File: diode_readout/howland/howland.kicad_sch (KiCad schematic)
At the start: 8 parts, among them J1 Conn_01x04, J2 JST_SH_Conn_01x04_i2c_horizon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

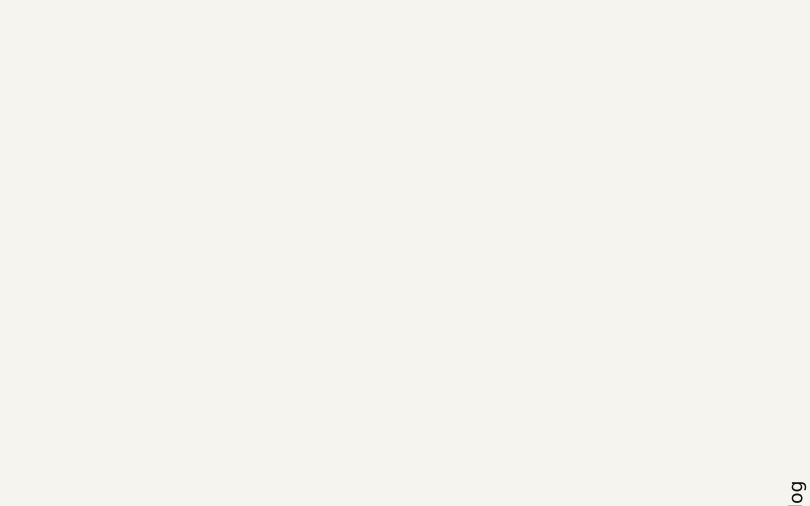
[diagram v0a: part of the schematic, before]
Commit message: add sq_lockin_v8 and tweaks to howland diode_readout
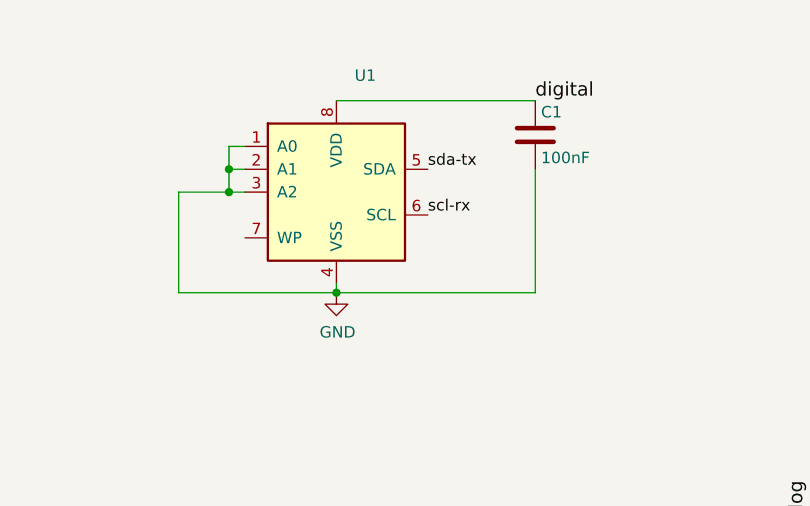
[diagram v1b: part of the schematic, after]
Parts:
- added C1: 100nF, Capacitor_SMD:C_0402_1005Metric, symbol Device:C
- added U1: (no value), symbol Memory_NVRAM:FM24C64C
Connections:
- net GND: now also U1.1 (A0), U1.2 (A1), U1.3 (A2), U1.4 (VSS)
- net VD: now also C1.1, U1.8 (VDD)
- net scl-rx: now also U1.6 (SCL)
- net sda-tx: now also U1.5 (SDA)

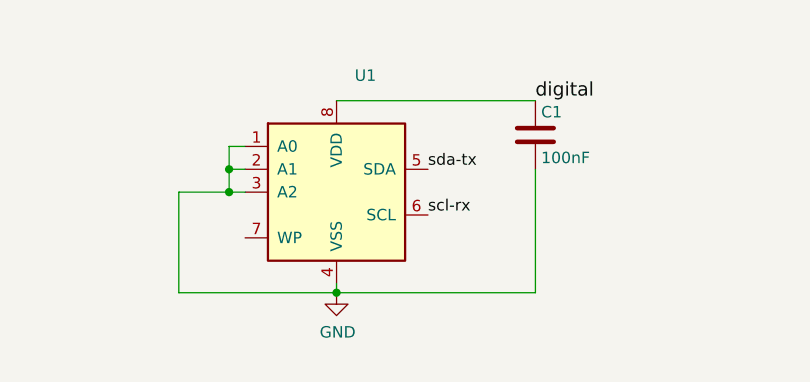
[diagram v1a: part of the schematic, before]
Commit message: Commit changes to howland current source diode readout: 1.  Add 1Mohm shorts bettern V+ and I+  as well as V- and I- to mimic      this will mimic the two wire readout behaviour when the diode gets      disconnected. 2.  Add FRAM chip, 512kbits or 64kBytes of memory
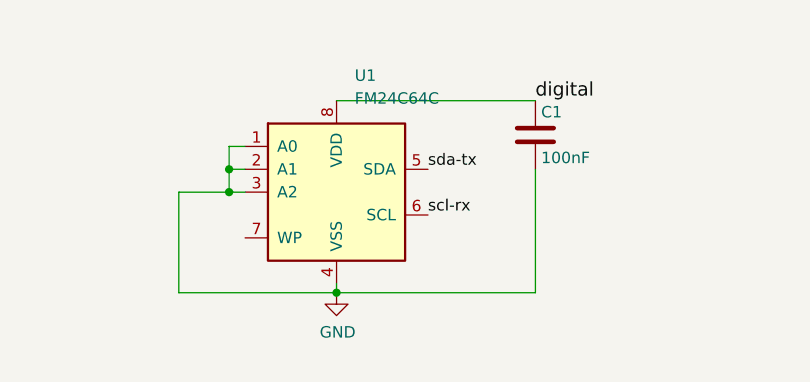
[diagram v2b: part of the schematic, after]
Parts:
- U1: value (none) -> FM24C64C; footprint (none) -> Package_SO:SOIC-8_3.9x4.9mm_P1.27mm
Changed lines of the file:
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@@
       (effects (font (size 1.27 1.27)) (justify left))
     )
-    (property "Value" "" (id 1) (at 110.9854 35.56 0)
+    (property "Value" "FM24C64C" (id 1) (at 110.9854 35.56 0)
       (effects (font (size 1.27 1.27)) (justify left))
     )
-    (property "Footprint" "" (id 2) (at 108.966 45.974 0)
+    (property "Footprint" "Package_SO:SOIC-8_3.9x4.9mm_P1.27mm" (id 2) (at 108.966 45.974 0)
       (effects (font (size 1.27 1.27)) hide)
     )
@@
       (reference "R2") (unit 1) (value "10K") (footprint "Resistor_SMD:R_0603_1608Metric_Pad1.05x0.95mm_HandSolder")
     )
+    (path "/00000000-0000-0000-0000-000059ed3d7b/cb59bfe4-78b3-4525-a18e-6016f07a38e4"
+      (reference "R3") (unit 1) (value "1M") (footprint "Resistor_SMD:R_0402_1005Metric")
+    )
+    (path "/00000000-0000-0000-0000-000059ed3d7b/393f0e56-c2d5-4ea4-8463-50265bc94d2d"
+      (reference "R4") (unit 1) (value "1M") (footprint "Resistor_SMD:R_0402_1005Metric")
+    )
     (path "/00000000-0000-0000-0000-000059ed3d7b/00000000-0000-0000-0000-000059ed1265"
-      (reference "R3") (unit 1) (value "100K") (footprint "Resistor_SMD:R_0402_1005Metric")
+      (reference "R5") (unit 1) (value "100K") (footprint "Resistor_SMD:R_0402_1005Metric")
     )
     (path "/00000000-0000-0000-0000-000059ed3d7b/00000000-0000-0000-0000-000059ed126c"
-      (reference "R4") (unit 1) (value "100K") (footprint "Resistor_SMD:R_0402_1005Metric")
+      (reference "R6") (unit 1) (value "100K") (footprint "Resistor_SMD:R_0402_1005Metric")
     )
     (path "/00000000-0000-0000-0000-000059ed3d7b/0a00994f-3fc0-414a-8e46-3a4bdcea5eb2/5aa91f3c-0195-4e75-88c2-51064725621d"
-      (reference "R5") (unit 1) (value "10K") (footprint "Resistor_SMD:R_0805_2012Metric")
+      (reference "R7") (unit 1) (value "10K") (footprint "Resistor_SMD:R_0805_2012Metric")
     )
     (path "/00000000-0000-0000-0000-000059ed3d7b/0a00994f-3fc0-414a-8e46-3a4bdcea5eb2/cc9e71ff-e12c-4106-95ad-954289c2f7e3"
-      (reference "R6") (unit 1) (value "10K") (footprint "Resistor_SMD:R_0805_2012Metric")
+      (reference "R8") (unit 1) (value "10K") (footprint "Resistor_SMD:R_0805_2012Metric")
     )
     (path "/00000000-0000-0000-0000-000059ed3d7b/0a00994f-3fc0-414a-8e46-3a4bdcea5eb2/a90a73b8-661a-4ba5-948b-2c2ada5eb5a5"
-      (reference "R7") (unit 1) (value "125K") (footprint "Resistor_SMD:R_0805_2012Metric")
+      (reference "R9") (unit 1) (value "125K") (footprint "Resistor_SMD:R_0805_2012Metric")
     )
     (path "/00000000-0000-0000-0000-000059ed3d7b/0a00994f-3fc0-414a-8e46-3a4bdcea5eb2/3430e4dd-38e6-4a37-ae77-90080133b97b"
-      (reference "R8") (unit 1) (value "12.7M") (footprint "Resistor_SMD:R_0805_2012Metric")
+      (reference "R10") (unit 1) (value "12.7M") (footprint "Resistor_SMD:R_0805_2012Metric")
     )
     (path "/00000000-0000-0000-0000-000059ed3d7b/0a00994f-3fc0-414a-8e46-3a4bdcea5eb2/5d00d18b-d30c-4aba-8513-d532618dc371"
-      (reference "R9") (unit 1) (value "10K") (footprint "Resistor_SMD:R_0805_2012Metric")
+      (reference "R11") (unit 1) (value "10K") (footprint "Resistor_SMD:R_0805_2012Metric")
     )
     (path "/00000000-0000-0000-0000-000059ed3d7b/0a00994f-3fc0-414a-8e46-3a4bdcea5eb2/63c4fe4d-2f4e-4b3c-a990-4f916aa9930d"
-      (reference "R10") (unit 1) (value "0") (footprint "Resistor_SMD:R_0603_1608Metric_Pad0.98x0.95mm_HandSolder")
+      (reference "R12") (unit 1) (value "0") (footprint "Resistor_SMD:R_0603_1608Metric_Pad0.98x0.95mm_HandSolder")
     )
     (path "/00000000-0000-0000-0000-000059ed3d7b/0a00994f-3fc0-414a-8e46-3a4bdcea5eb2/4c7508f6-a275-40c9-9d80-35a0598d72c4"
@@
       (reference "U3") (unit 3) (value "TLV2782IDGKR") (footprint "Package_SO:VSSOP-8_3.0x3.0mm_P0.65mm")
     )
-    (path "/00000000-0000-0000-0000-000059ed3d7b/0a00994f-3fc0-414a-8e46-3a4bdcea5eb2/5cbea609-3336-48c5-807b-8f275a8e6dc1"
-      (reference "U4") (unit 1) (value "REF3225AMDBVREP") (footprint "Package_TO_SOT_SMD:SOT-23-6")
+    (path "/00000000-0000-0000-0000-000059ed3d7b/0a00994f-3fc0-414a-8e46-3a4bdcea5eb2/3ccb3e27-d022-4f68-b9b2-be66e341ab1b"
+      (reference "U4") (unit 1) (value "ADR391") (footprint "Package_TO_SOT_SMD:TSOT-23-5_HandSoldering")
     )
     (path "/00000000-0000-0000-0000-000059ed3d7b/0a00994f-3fc0-414a-8e46-3a4bdcea5eb2/d62bbf6c-bcf2-4b7a-9470-80c869ae73db"

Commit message: Keep boards up to date
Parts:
- U1: value FM24C64C -> (none); footprint Package_SO:SOIC-8_3.9x4.9mm_P1.27mm -> (none)
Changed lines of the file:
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@@
       (effects (font (size 1.27 1.27)) (justify left))
     )
-    (property "Value" "FM24C64C" (id 1) (at 110.9854 35.56 0)
+    (property "Value" "" (id 1) (at 110.9854 35.56 0)
       (effects (font (size 1.27 1.27)) (justify left))
     )
-    (property "Footprint" "Package_SO:SOIC-8_3.9x4.9mm_P1.27mm" (id 2) (at 108.966 45.974 0)
-      (effects (font (size 1.27 1.27)) hide)
-    )
-    (property "Datasheet" "http://www.cypress.com/file/41651/download" (id 3) (at 103.886 37.084 0)
+    (property "Footprint" "" (id 2) (at 108.966 45.974 0)
+      (effects (font (size 1.27 1.27)) hide)
+    )
+    (property "Datasheet" "https://datasheet.lcsc.com/lcsc/1806121739_Cypress-Semicon-FM24V05-GTR_C66021.pdf" (id 3) (at 103.886 37.084 0)
       (effects (font (size 1.27 1.27)) hide)
     )
@@
     )
     (path "/ab88f3e0-e707-48e0-91f8-7ac28f1ec265"
-      (reference "U1") (unit 1) (value "FM24C64C") (footprint "Package_SO:SOIC-8_3.9x4.9mm_P1.27mm")
+      (reference "U1") (unit 1) (value "FM24V05") (footprint "Package_SO:SOIC-8_3.9x4.9mm_P1.27mm")
     )
     (path "/00000000-0000-0000-0000-000059ed3d7b/e9890516-b047-4c9e-9731-dd57dc45efd4"

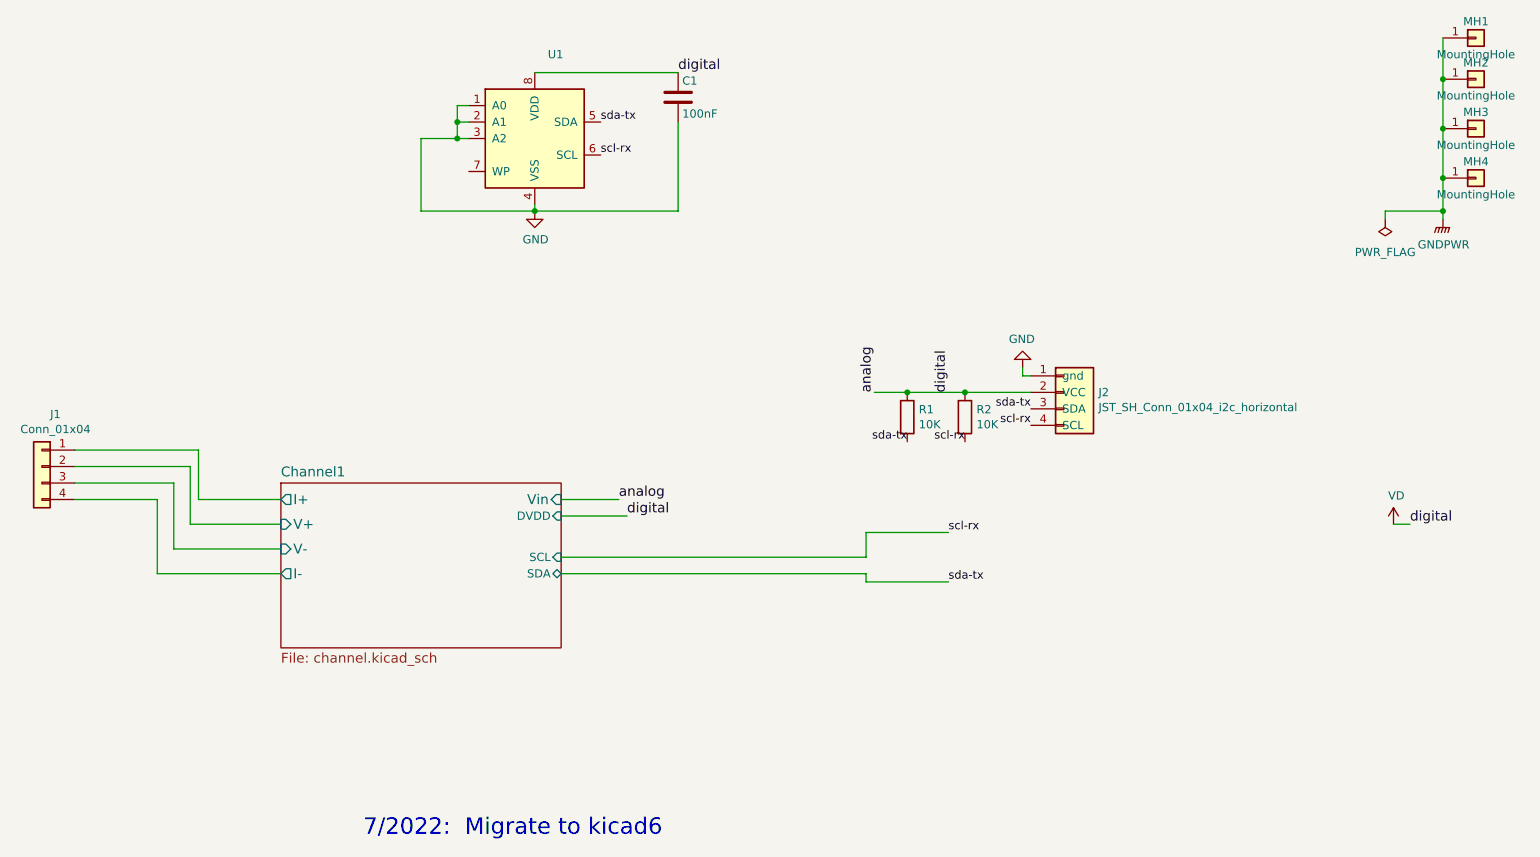
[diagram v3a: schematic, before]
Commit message: Add tweaks to diode readout
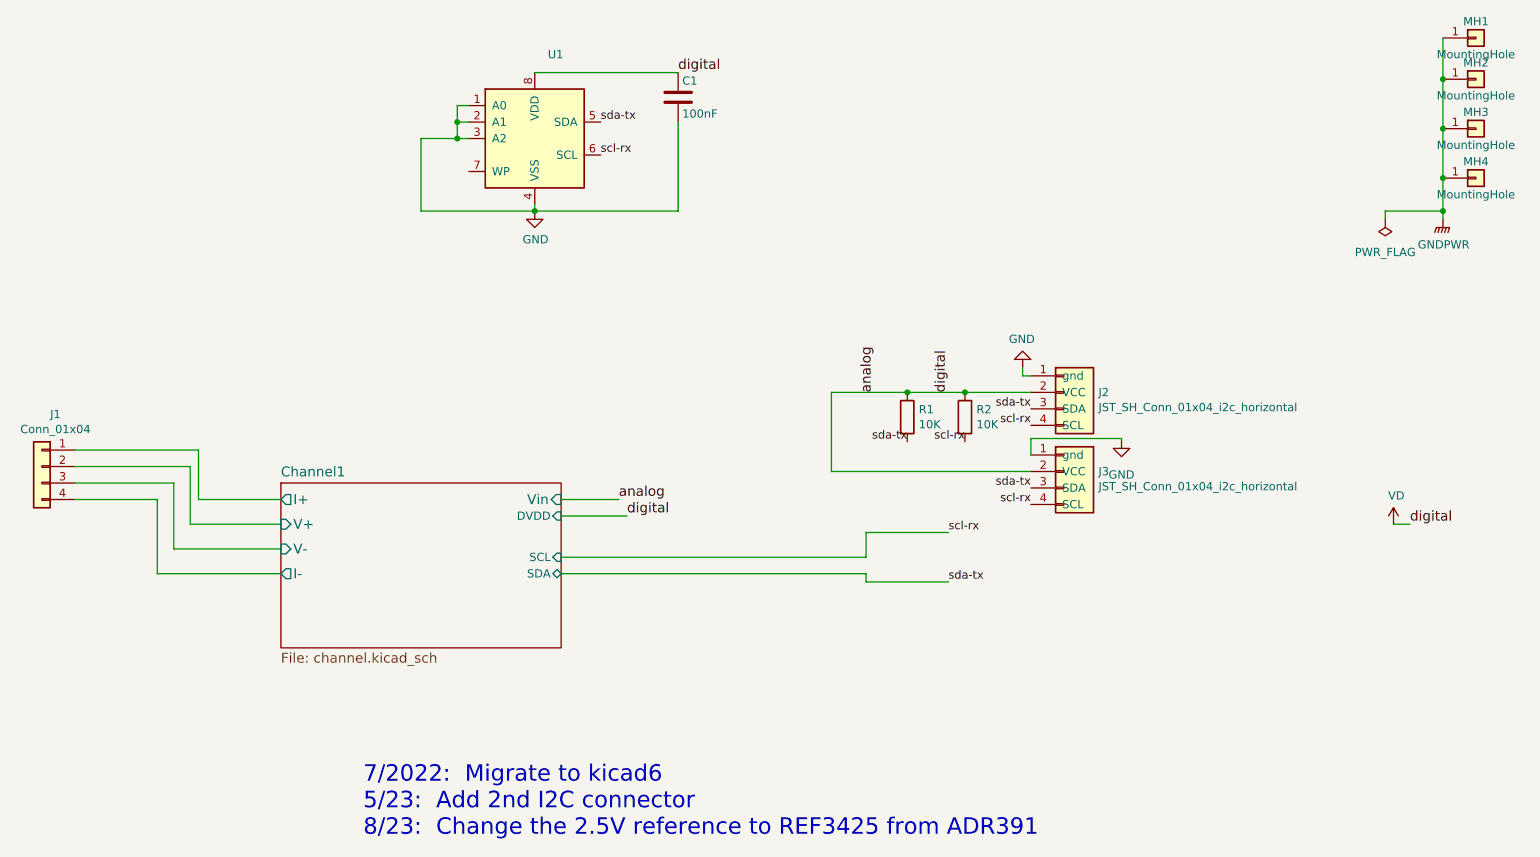
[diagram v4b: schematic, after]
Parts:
- added J3: JST_SH_Conn_01x04_i2c_horizontal, Connector_JST:JST_SH_SM04B-SRSS-TB_1x04-1MP_P1.00mm_Horizontal, symbol 0JLC-6:JST_SH_Conn_01x04_i2c_horizontal
- U1: LCSC (none) -> C66021
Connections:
- net GND: now also J3.1 (gnd)
- net VD: now also J3.2 (VCC)
- net scl-rx: now also J3.4 (SCL)
- net sda-tx: now also J3.3 (SDA)
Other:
- note added: "7/2022: Migrate to kicad6 5/23: Add 2nd I2C connector 8/23: Change the 2.5V reference to REF3425 from ADR391"
- note removed: "7/2022: Migrate to kicad6"
